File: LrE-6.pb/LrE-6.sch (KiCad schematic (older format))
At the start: 110 parts, among them J1 USB_B_Micro, J2 SM06B-SRSS-TB, Q1 2N7002, SW1 SW_Push_45deg, SW10 SW_Push_45deg, SW11 Rotary_Encoder_Switch, SW12 Rotary_Encoder_Switch, SW13 Rotary_Encoder_Switch, SW14 Rotary_Encoder_Switch, SW15 Rotary_Encoder_Switch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

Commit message: 0.28-5
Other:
- note added: "F2.2\n"
- note removed: "R2.2\n"
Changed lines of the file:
@@
 EESchema Schematic File Version 4
-LIBS:LrE-6-cache
-EELAYER 29 0
+EELAYER 30 0
 EELAYER END
 $Descr A3 16535 11693
@@
 Wire Wire Line
 	11650 1700 11650 1650
-Text Notes 15300 9850 0    197  ~ 0
-R2.2\n
+Text Notes 15200 10450 0    197  ~ 0
+F2.2\n
 Wire Wire Line
 	1200 10900 1700 10900

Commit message: 0.28-6
change Rotary Encoder from 9.5KQ to 'symmetry hole' model.
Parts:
- SW11, SW12, SW13, SW14, SW15, SW16: footprint LrE-6:RotaryEncoder_EC11E-SMD -> LrE-6:RotaryEncoder_EC11E-SMD2
- TP1: footprint TestPoint:TestPoint_THTPad_D1.5mm_Drill0.7mm -> TestPoint:TestPoint_THTPad_D1.0mm_Drill0.5mm
- TP2, TP3: footprint TestPoint:TestPoint_THTPad_D2.0mm_Drill1.0mm -> TestPoint:TestPoint_THTPad_D1.0mm_Drill0.5mm
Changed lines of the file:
@@
 F 0 "SW11" H 2300 1817 50  0000 C CNN
 F 1 "Rotary_Encoder_Switch" H 2300 1726 50  0000 C CNN
-F 2 "LrE-6:RotaryEncoder_EC11E-SMD" H 2150 1610 50  0001 C CNN
+F 2 "LrE-6:RotaryEncoder_EC11E-SMD2" H 2150 1610 50  0001 C CNN
 F 3 "~" H 2300 1710 50  0001 C CNN
 	1    2300 1450
@@
 F 0 "SW12" H 2350 3467 50  0000 C CNN
 F 1 "Rotary_Encoder_Switch" H 2350 3376 50  0000 C CNN
-F 2 "LrE-6:RotaryEncoder_EC11E-SMD" H 2200 3260 50  0001 C CNN
+F 2 "LrE-6:RotaryEncoder_EC11E-SMD2" H 2200 3260 50  0001 C CNN
 F 3 "~" H 2350 3360 50  0001 C CNN
 	1    2350 3100
@@
 F 0 "SW13" H 2450 5217 50  0000 C CNN
 F 1 "Rotary_Encoder_Switch" H 2450 5126 50  0000 C CNN
-F 2 "LrE-6:RotaryEncoder_EC11E-SMD" H 2300 5010 50  0001 C CNN
+F 2 "LrE-6:RotaryEncoder_EC11E-SMD2" H 2300 5010 50  0001 C CNN
 F 3 "~" H 2450 5110 50  0001 C CNN
 	1    2450 4850
@@
 F 0 "SW14" H 5000 1767 50  0000 C CNN
 F 1 "Rotary_Encoder_Switch" H 5000 1676 50  0000 C CNN
-F 2 "LrE-6:RotaryEncoder_EC11E-SMD" H 4850 1560 50  0001 C CNN
+F 2 "LrE-6:RotaryEncoder_EC11E-SMD2" H 4850 1560 50  0001 C CNN
 F 3 "~" H 5000 1660 50  0001 C CNN
 	1    5000 1400
@@
 F 0 "SW15" H 5150 3467 50  0000 C CNN
 F 1 "Rotary_Encoder_Switch" H 5150 3376 50  0000 C CNN
-F 2 "LrE-6:RotaryEncoder_EC11E-SMD" H 5000 3260 50  0001 C CNN
+F 2 "LrE-6:RotaryEncoder_EC11E-SMD2" H 5000 3260 50  0001 C CNN
 F 3 "~" H 5150 3360 50  0001 C CNN
 	1    5150 3100
@@
 F 0 "SW16" H 5250 5217 50  0000 C CNN
 F 1 "Rotary_Encoder_Switch" H 5250 5126 50  0000 C CNN
-F 2 "LrE-6:RotaryEncoder_EC11E-SMD" H 5100 5010 50  0001 C CNN
+F 2 "LrE-6:RotaryEncoder_EC11E-SMD2" H 5100 5010 50  0001 C CNN
 F 3 "~" H 5250 5110 50  0001 C CNN
 	1    5250 4850
@@
 F 0 "TP1" H 13408 2518 50  0000 L CNN
 F 1 "TestPoint" H 13408 2427 50  0000 L CNN
-F 2 "TestPoint:TestPoint_THTPad_D1.5mm_Drill0.7mm" H 13550 2400 50  0001 C CNN
+F 2 "TestPoint:TestPoint_THTPad_D1.0mm_Drill0.5mm" H 13550 2400 50  0001 C CNN
 F 3 "~" H 13550 2400 50  0001 C CNN
 	1    13350 2400
@@
 F 0 "TP3" H 12800 7200 50  0000 L CNN
 F 1 "TestPoint-Connector" H 12858 6977 50  0001 L CNN
-F 2 "TestPoint:TestPoint_THTPad_D2.0mm_Drill1.0mm" H 13000 6950 50  0001 C CNN
+F 2 "TestPoint:TestPoint_THTPad_D1.0mm_Drill0.5mm" H 13000 6950 50  0001 C CNN
 F 3 "" H 13000 6950 50  0001 C CNN
 	1    12800 6950
@@
 F 0 "TP2" H 12600 7200 50  0000 L CNN
 F 1 "TestPoint-Connector" H 12758 6977 50  0001 L CNN
-F 2 "TestPoint:TestPoint_THTPad_D2.0mm_Drill1.0mm" H 12900 6950 50  0001 C CNN
+F 2 "TestPoint:TestPoint_THTPad_D1.0mm_Drill0.5mm" H 12900 6950 50  0001 C CNN
 F 3 "" H 12900 6950 50  0001 C CNN
 	1    12700 6950

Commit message: 0.28-7
F2.2 PCB ordered.
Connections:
- wire segments 429 -> 426
- no-connect marks 14 -> 15
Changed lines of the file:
@@
 Wire Wire Line
 	13000 8200 13000 8350
-$Comp
-L LrE-6-rescue:GND-power #PWR01
-U 1 1 5E527AC2
-P 13700 7850
-F 0 "#PWR01" H 13700 7600 50  0001 C CNN
-F 1 "GND" H 13850 7750 50  0000 C CNN
-F 2 "" H 13700 7850 50  0001 C CNN
-F 3 "" H 13700 7850 50  0001 C CNN
-	1    13700 7850
-	1    0    0    -1
-$EndComp
 Wire Wire Line
 	13450 7250 13900 7250
 Connection ~ 13450 7250
-Wire Wire Line
-	13900 7850 13700 7850
 Connection ~ 13450 6150
 $Comp
@@
 	14650 6550 14750 6550
 NoConn ~ 9100 5250
-Wire Wire Line
-	13700 7850 13700 7000
-Wire Wire Line
-	13700 7000 13900 7000
-Connection ~ 13700 7850
 $Comp
 L LrE-6:OLED-0.91 U3
@@
 Wire Wire Line
 	12800 7400 13200 7400
+NoConn ~ 15100 8150
 $EndSCHEMATC

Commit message: 0.32
F2.2 PB first run
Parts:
- C28, C29: value 2.2u -> 10u
- R18: value 390K -> 62
- R19, R20: footprint Resistor_SMD:R_0603_1608Metric -> Resistor_SMD:R_0805_2012Metric
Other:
- note added: "F2.4"
- note removed: "F2.2\n"
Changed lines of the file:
@@
 EESchema Schematic File Version 4
-EELAYER 30 0
+LIBS:LrE-6-cache
+EELAYER 29 0
 EELAYER END
 $Descr A3 16535 11693
@@
 F 0 "R19" V 13100 6350 50  0000 L CNN
 F 1 "10K" V 13100 6550 50  0000 L CNN
-F 2 "Resistor_SMD:R_0603_1608Metric" V 13130 6550 50  0001 C CNN
+F 2 "Resistor_SMD:R_0805_2012Metric" V 13130 6550 50  0001 C CNN
 F 3 "~" H 13200 6550 50  0001 C CNN
 	1    13200 6550
@@
 F 0 "R20" V 13350 6350 50  0000 L CNN
 F 1 "10K" V 13350 6550 50  0000 L CNN
-F 2 "Resistor_SMD:R_0603_1608Metric" V 13380 6550 50  0001 C CNN
+F 2 "Resistor_SMD:R_0805_2012Metric" V 13380 6550 50  0001 C CNN
 F 3 "~" H 13450 6550 50  0001 C CNN
 	1    13450 6550
@@
 P 15200 8700
 F 0 "R18" V 15300 8800 50  0000 C CNN
-F 1 "390K" V 15300 8600 50  0000 C CNN
+F 1 "62" V 15300 8600 50  0000 C CNN
 F 2 "Resistor_SMD:R_0805_2012Metric" V 15130 8700 50  0001 C CNN
 F 3 "~" H 15200 8700 50  0001 C CNN
@@
 	11650 1700 11650 1650
 Text Notes 15200 10450 0    197  ~ 0
-F2.2\n
+F2.4
 Wire Wire Line
 	1200 10900 1700 10900
@@
 P 15800 8950
 F 0 "C28" H 15600 8800 50  0000 L CNN
-F 1 "2.2u" H 15550 9050 50  0000 L CNN
+F 1 "10u" H 15550 9050 50  0000 L CNN
 F 2 "Capacitor_SMD:C_0805_2012Metric" H 15838 8800 50  0001 C CNN
 F 3 "~" H 15800 8950 50  0001 C CNN
@@
 P 15500 8950
 F 0 "C29" H 15300 8800 50  0000 L CNN
-F 1 "2.2u" H 15300 9050 50  0000 L CNN
+F 1 "10u" H 15300 9050 50  0000 L CNN
 F 2 "Capacitor_SMD:C_0805_2012Metric" H 15538 8800 50  0001 C CNN
 F 3 "~" H 15500 8950 50  0001 C CNN

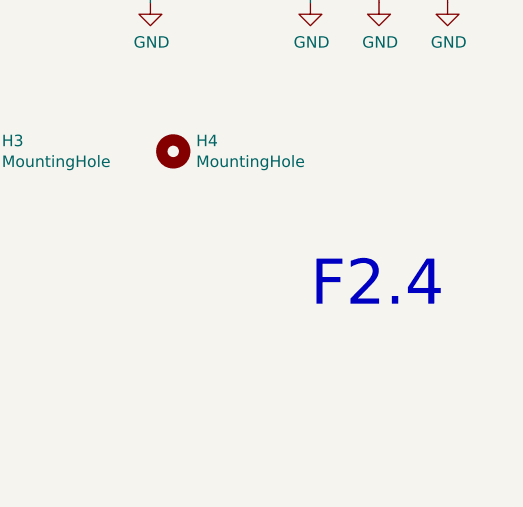
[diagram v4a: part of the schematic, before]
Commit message: 0.32-1
Fixed SSD1306 Horizontal paging initialize
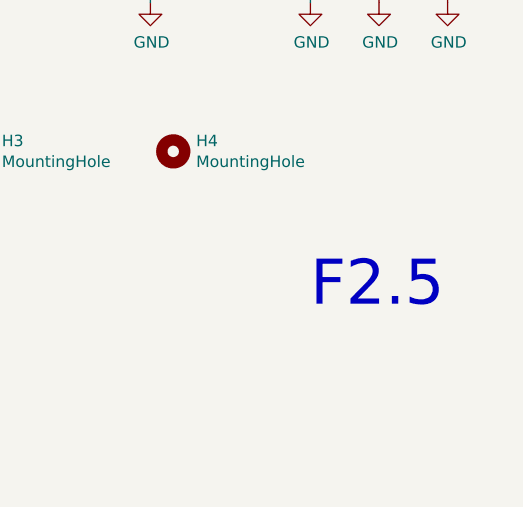
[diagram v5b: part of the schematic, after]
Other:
- note added: "F2.5"
- note removed: "F2.4"
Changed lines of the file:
@@
 EESchema Schematic File Version 4
-LIBS:LrE-6-cache
-EELAYER 29 0
+EELAYER 30 0
 EELAYER END
 $Descr A3 16535 11693
@@
 	11650 1700 11650 1650
 Text Notes 15200 10450 0    197  ~ 0
-F2.4
+F2.5
 Wire Wire Line
 	1200 10900 1700 10900

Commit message: 0.33-5
F2.8 board
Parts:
- removed TP2, TP3: TestPoint-Connector, TestPoint:TestPoint_THTPad_D1.0mm_Drill0.5mm, symbol LrE-6-rescue:TestPoint-Connector
- D18: value LED GR -> LED0603_WH
- D31, D32, D33, D34, D35, D36: value WS2812B -> WS2812B-2020
- R21: value 4.7K -> 10K
- R24: value 470 -> 1K
- SW1, SW10, SW2, SW3, SW4, SW5, SW6, SW7, SW8, SW9: value SW_Push_45deg -> Tact_SW_8mm
- SW11, SW12, SW13, SW14, SW15, SW16: value Rotary_Encoder_Switch -> EC11_SMD
- U3: value OLED-0.91 -> SSD1306_OLED_0.91
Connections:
- wire segments 426 -> 422
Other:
- note added: "F2.8"
- note removed: "F2.5"
- moved on the sheet: R24, TP1

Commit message: 0.34-1
modify comments for doxygen
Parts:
- C15, C19, C28, C29: value 10u -> 4.7u
- D18: value LED0603_WH -> LED0603_BL
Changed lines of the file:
@@
 EESchema Schematic File Version 4
-LIBS:LrE-6-cache
-EELAYER 29 0
+EELAYER 30 0
 EELAYER END
 $Descr A3 16535 11693
@@
 P 9000 1400
 F 0 "C15" V 8950 1200 50  0000 C CNN
-F 1 "10u" V 8950 1550 50  0000 C CNN
+F 1 "4.7u" V 8950 1550 50  0000 C CNN
 F 2 "Capacitor_SMD:C_0805_2012Metric" H 9038 1250 50  0001 C CNN
 F 3 "~" H 9000 1400 50  0001 C CNN
@@
 P 9000 2400
 F 0 "C19" V 8950 2200 50  0000 C CNN
-F 1 "10u" V 8950 2550 50  0000 C CNN
+F 1 "4.7u" V 8950 2550 50  0000 C CNN
 F 2 "Capacitor_SMD:C_0805_2012Metric" H 9038 2250 50  0001 C CNN
 F 3 "~" H 9000 2400 50  0001 C CNN
@@
 P 14150 2450
 F 0 "D18" H 14141 2666 50  0000 C CNN
-F 1 "LED0603_WH" H 14141 2575 50  0000 C CNN
+F 1 "LED0603_BL" H 14141 2575 50  0000 C CNN
 F 2 "LED_SMD:LED_0603_1608Metric" H 14150 2450 50  0001 C CNN
 F 3 "~" H 14150 2450 50  0001 C CNN
@@
 P 15800 8950
 F 0 "C28" H 15600 8800 50  0000 L CNN
-F 1 "10u" H 15550 9050 50  0000 L CNN
+F 1 "4.7u" H 15550 9050 50  0000 L CNN
 F 2 "Capacitor_SMD:C_0805_2012Metric" H 15838 8800 50  0001 C CNN
 F 3 "~" H 15800 8950 50  0001 C CNN
@@
 P 15500 8950
 F 0 "C29" H 15300 8800 50  0000 L CNN
-F 1 "10u" H 15300 9050 50  0000 L CNN
+F 1 "4.7u" H 15300 9050 50  0000 L CNN
 F 2 "Capacitor_SMD:C_0805_2012Metric" H 15538 8800 50  0001 C CNN
 F 3 "~" H 15500 8950 50  0001 C CNN

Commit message: 0.37-6
Fix pb for OLED stability.
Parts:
- added R22: 1K, Resistor_SMD:R_0805_2012Metric, symbol Device:R
- added R23: 100, Resistor_SMD:R_0805_2012Metric, symbol Device:R
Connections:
- wire segments 422 -> 427
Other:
- note added: "F2.8-1"
- note removed: "F2.8"
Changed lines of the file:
@@
 L LrE-6-rescue:+3V3-power #PWR0119
 U 1 1 5C4EAC46
-P 13200 6050
-F 0 "#PWR0119" H 13200 5900 50  0001 C CNN
-F 1 "+3V3" H 13215 6223 50  0000 C CNN
-F 2 "" H 13200 6050 50  0001 C CNN
-F 3 "" H 13200 6050 50  0001 C CNN
-	1    13200 6050
+P 13200 5450
+F 0 "#PWR0119" H 13200 5300 50  0001 C CNN
+F 1 "+3V3" H 13215 5623 50  0000 C CNN
+F 2 "" H 13200 5450 50  0001 C CNN
+F 3 "" H 13200 5450 50  0001 C CNN
+	1    13200 5450
 	1    0    0    -1
 $EndComp
@@
 $EndComp
 Wire Wire Line
-	13450 6400 13450 6150
-Wire Wire Line
-	13450 6150 13200 6150
-Wire Wire Line
-	13200 6150 13200 6050
-Wire Wire Line
-	13200 6400 13200 6150
-Connection ~ 13200 6150
+	13450 6400 13450 5500
 Text Label 12500 7250 0    50   ~ 0
 SDA
@@
 Wire Wire Line
 	11650 1700 11650 1650
-Text Notes 15200 10450 0    197  ~ 0
-F2.8
+Text Notes 14900 10450 0    197  ~ 0
+F2.8-1
 Wire Wire Line
 	1200 10900 1700 10900
@@
 	13450 7250 13900 7250
 Connection ~ 13450 7250
-Connection ~ 13450 6150
 $Comp
 L LrE-6-rescue:C-Device C28
@@
 	1    0    0    -1
 $EndComp
-Wire Wire Line
-	14650 6150 14400 6150
-Connection ~ 14400 6150
-Wire Wire Line
-	13450 6150 14400 6150
 $Comp
 L LrE-6-rescue:C-Device C27
@@
 	15100 7250 15800 7250
 Wire Wire Line
-	14400 6150 14400 6400
-Wire Wire Line
-	14650 6150 14650 6550
+	14650 5500 14650 6550
 Wire Wire Line
 	15050 6550 15250 6550
@@
 Wire Wire Line
 	14200 6400 14400 6400
-Connection ~ 14400 6400
 Wire Wire Line
 	14400 6400 14400 6800
@@
 Wire Wire Line
 	12500 7400 13200 7400
+Wire Wire Line
+	13200 6400 13200 5500
+$Comp
+L Device:R R23
+U 1 1 5EEE6BD3
+P 14400 5850
+F 0 "R23" H 14150 5950 50  0000 L CNN
+F 1 "100" H 14150 5850 50  0000 L CNN
+F 2 "Resistor_SMD:R_0805_2012Metric" V 14330 5850 50  0001 C CNN
+F 3 "~" H 14400 5850 50  0001 C CNN
+	1    14400 5850
+	1    0    0    -1
+$EndComp
+$Comp
+L Device:R R22
+U 1 1 5EEE73A1
+P 14050 6150
+F 0 "R22" V 13843 6150 50  0000 C CNN
+F 1 "1K" V 13934 6150 50  0000 C CNN
+F 2 "Resistor_SMD:R_0805_2012Metric" V 13980 6150 50  0001 C CNN
+F 3 "~" H 14050 6150 50  0001 C CNN
+	1    14050 6150
+	0    1    1    0
+$EndComp
+Wire Wire Line
+	14400 6000 14400 6150
+Connection ~ 14400 6400
+Wire Wire Line
+	14200 6150 14400 6150
+Connection ~ 14400 6150
+Wire Wire Line
+	14400 6150 14400 6400
+Wire Wire Line
+	13900 6150 13750 6150
+Wire Wire Line
+	13750 6150 13750 6400
+Connection ~ 13750 6400
+Wire Wire Line
+	13200 5500 13450 5500
+Connection ~ 13200 5500
+Wire Wire Line
+	13200 5500 13200 5450
+Connection ~ 13450 5500
+Wire Wire Line
+	13450 5500 14400 5500
+Wire Wire Line
+	14400 5700 14400 5500
+Connection ~ 14400 5500
+Wire Wire Line
+	14400 5500 14650 5500
 $EndSCHEMATC
